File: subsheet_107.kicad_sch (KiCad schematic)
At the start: 17 parts, among them T12 BDX54

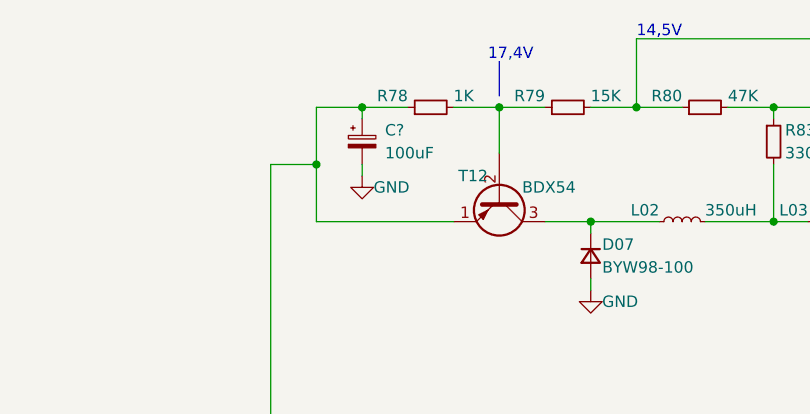
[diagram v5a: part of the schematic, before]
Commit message: fixes DRC : duplicate, designators with '?'
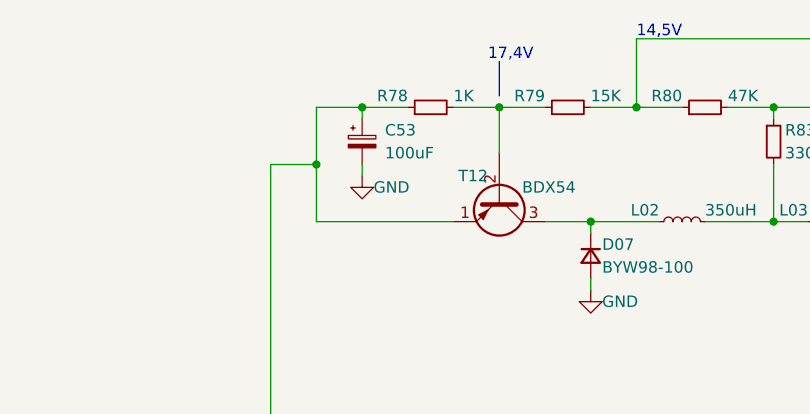
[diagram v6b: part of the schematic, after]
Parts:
- gave numbers to parts that had none: 1
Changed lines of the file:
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@@
   (symbol (lib_id "power-custom:+18V") (at 154.94 93.98 0) (unit 1)
     (in_bom yes) (on_board yes)
-    (property "Reference" "#PWR?" (id 0) (at 154.94 97.79 0)
+    (property "Reference" "#PWR0283" (id 0) (at 154.94 97.79 0)
       (effects (font (size 1.27 1.27)) hide)
     )
@@
   (symbol (lib_id "power:GND") (at 76.2 111.76 0) (unit 1)
     (in_bom yes) (on_board yes)
-    (property "Reference" "#PWR?" (id 0) (at 76.2 118.11 0)
+    (property "Reference" "#PWR0287" (id 0) (at 76.2 118.11 0)
       (effects (font (size 1.27 1.27)) hide)
     )
@@
   (symbol (lib_id "power-custom:+18V") (at 55.88 101.6 0) (unit 1)
     (in_bom yes) (on_board yes)
-    (property "Reference" "#PWR?" (id 0) (at 55.88 105.41 0)
+    (property "Reference" "#PWR0286" (id 0) (at 55.88 105.41 0)
       (effects (font (size 1.27 1.27)) hide)
     )
@@
   (symbol (lib_id "Device:C_Polarized_Small") (at 76.2 50.8 0) (unit 1)
     (in_bom yes) (on_board yes)
-    (property "Reference" "C?" (id 0) (at 78.74 49.53 0)
+    (property "Reference" "C53" (id 0) (at 78.74 49.53 0)
       (effects (font (size 1.27 1.27)) (justify left))
     )
@@
   (symbol (lib_id "power:+5V") (at 143.51 59.69 0) (unit 1)
     (in_bom yes) (on_board yes)
-    (property "Reference" "#PWR?" (id 0) (at 143.51 63.5 0)
+    (property "Reference" "#PWR0289" (id 0) (at 143.51 63.5 0)
       (effects (font (size 1.27 1.27)) hide)
     )
@@
   (symbol (lib_id "power:PWR_FLAG") (at 137.16 59.69 180) (unit 1)
     (in_bom yes) (on_board yes)
-    (property "Reference" "#FLG?" (id 0) (at 137.16 61.595 0)
+    (property "Reference" "#FLG0101" (id 0) (at 137.16 61.595 0)
       (effects (font (size 1.27 1.27)) hide)
     )
@@
   (symbol (lib_id "power:GND") (at 46.99 96.52 0) (unit 1)
     (in_bom yes) (on_board yes)
-    (property "Reference" "#PWR?" (id 0) (at 46.99 102.87 0)
+    (property "Reference" "#PWR0288" (id 0) (at 46.99 102.87 0)
       (effects (font (size 1.27 1.27)) hide)
     )
@@
   (symbol (lib_id "power:GND") (at 153.67 57.15 0) (unit 1)
     (in_bom yes) (on_board yes)
-    (property "Reference" "#PWR?" (id 0) (at 153.67 63.5 0)
+    (property "Reference" "#PWR0291" (id 0) (at 153.67 63.5 0)
       (effects (font (size 1.27 1.27)) hide)
     )
@@
   (symbol (lib_id "power:PWR_FLAG") (at 41.91 96.52 0) (unit 1)
     (in_bom yes) (on_board yes)
-    (property "Reference" "#FLG?" (id 0) (at 41.91 94.615 0)
+    (property "Reference" "#FLG0102" (id 0) (at 41.91 94.615 0)
       (effects (font (size 1.27 1.27)) hide)
     )
@@
   (symbol (lib_id "power:GND") (at 76.2 54.61 0) (unit 1)
     (in_bom yes) (on_board yes)
-    (property "Reference" "#PWR?" (id 0) (at 76.2 60.96 0)
+    (property "Reference" "#PWR0285" (id 0) (at 76.2 60.96 0)
       (effects (font (size 1.27 1.27)) hide)
     )
@@
   (symbol (lib_id "power:GND") (at 143.51 72.39 0) (unit 1)
     (in_bom yes) (on_board yes)
-    (property "Reference" "#PWR?" (id 0) (at 143.51 78.74 0)
+    (property "Reference" "#PWR0290" (id 0) (at 143.51 78.74 0)
       (effects (font (size 1.27 1.27)) hide)
     )
@@
   (symbol (lib_id "power:PWR_FLAG") (at 50.8 101.6 180) (unit 1)
     (in_bom yes) (on_board yes)
-    (property "Reference" "#FLG?" (id 0) (at 50.8 103.505 0)
+    (property "Reference" "#FLG0103" (id 0) (at 50.8 103.505 0)
       (effects (font (size 1.27 1.27)) hide)
     )
@@
   (symbol (lib_id "power:GND") (at 101.6 67.31 0) (unit 1)
     (in_bom yes) (on_board yes)
-    (property "Reference" "#PWR?" (id 0) (at 101.6 73.66 0)
-      (effects (font (size 1.27 1.27)) hide)
-    )
+    (property "Reference" "#PWR0284" (id 0) (at 101.6 73.66 0)
+      (effects (font (size 1.27 1.27)) hide)
+    )

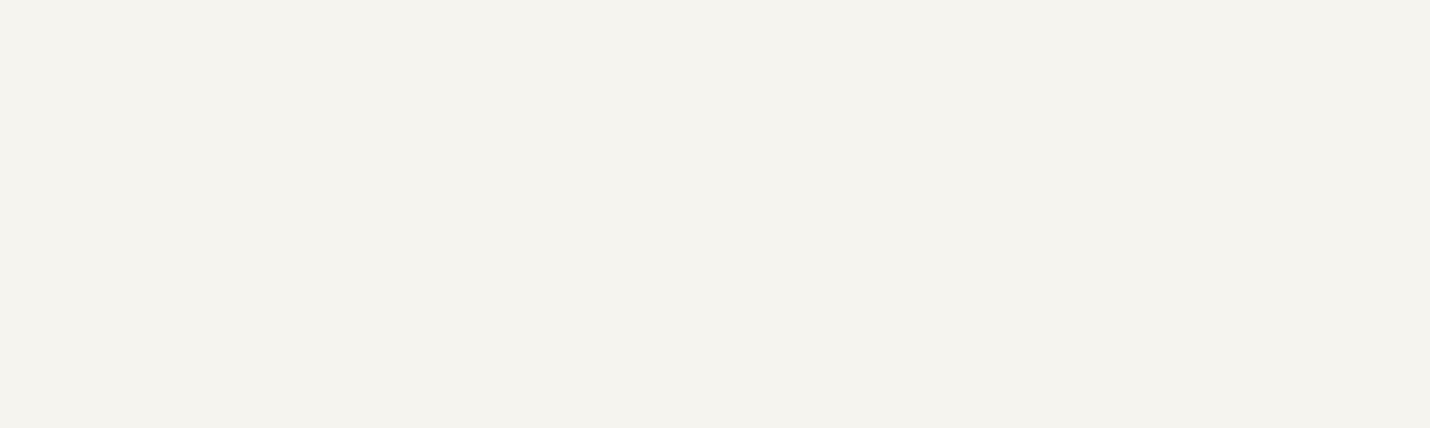
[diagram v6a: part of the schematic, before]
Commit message: schematic : mounting holes
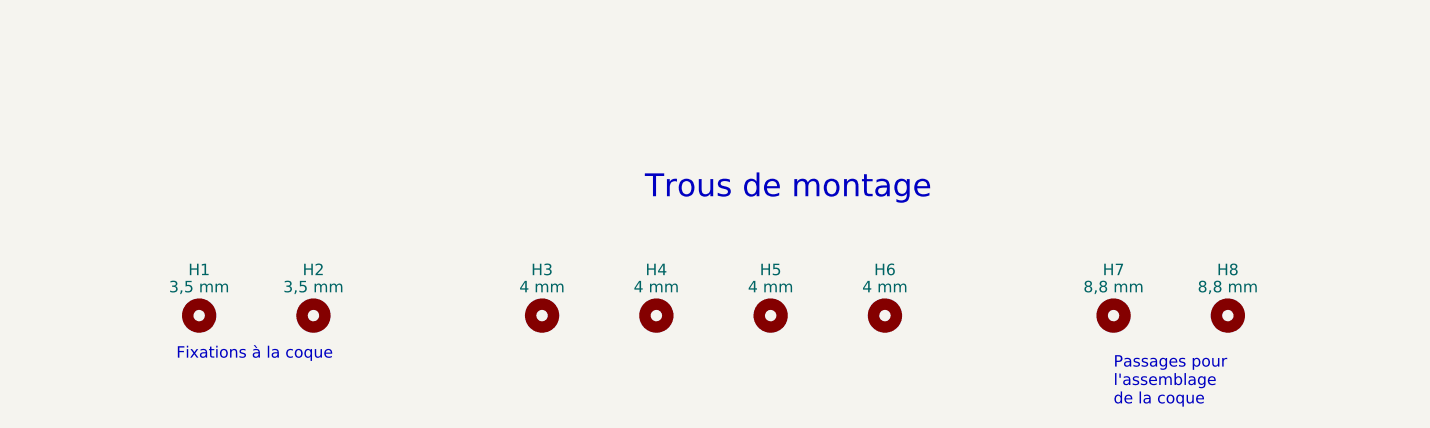
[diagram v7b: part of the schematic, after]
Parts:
- added H1, H2: 3,5 mm, mounting-holes-mo5:MountingHole_3.5mm_limited_courtyard, symbol Mechanical:MountingHole
- added H3, H4, H5, H6: 4 mm, mounting-holes-mo5:MountingHole_4mm_limited_courtyard, symbol Mechanical:MountingHole
- added H7, H8: 8,8 mm, mounting-holes-mo5:MountingHole_8.8mm_limited_courtyard, symbol Mechanical:MountingHole
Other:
- note added: "Fixations à la coque"
- note added: "Passages pour l'assemblage de la coque"
- note added: "Trous de montage"
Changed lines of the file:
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@@
     (effects (font (size 1.27 1.27)) (justify left bottom))
+  )
+  (text "Trous de montage" (at 87.63 203.2 0)
+    (effects (font (size 2.54 2.54)) (justify left bottom))
   )
   (text "17,4V" (at 90.17 41.91 0)
@@
     (effects (font (size 1.27 1.27)) (justify left bottom))
   )
+  (text "Fixations à la coque" (at 35.56 220.98 0)
+    (effects (font (size 1.27 1.27)) (justify left bottom))
+  )
   (text "5V" (at 83.82 104.14 0)
     (effects (font (size 1.27 1.27)) (justify left bottom))
@@
     (effects (font (size 1.27 1.27)) (justify right bottom))
   )
+  (text "Passages pour \nl'assemblage \nde la coque" (at 139.7 226.06 0)
+    (effects (font (size 1.27 1.27)) (justify left bottom))
+  )
   (text "5V" (at 107.95 99.06 180)
     (effects (font (size 1.27 1.27)) (justify right bottom))
@@
     )
     (pin "1")
+  )
+  (symbol (lib_id "Mechanical:MountingHole") (at 101.6 215.9 0) (unit 1)
+    (in_bom yes) (on_board yes)
+    (property "Reference" "H5" (id 0) (at 101.6 210.82 0))
+    (property "Value" "4 mm" (id 1) (at 101.6 212.725 0))
+    (property "Footprint" "mounting-holes-mo5:MountingHole_4mm_limited_courtyard" (id 2) (at 101.6 215.9 0)
+      (effects (font (size 1.27 1.27)) hide)
+    )
+    (property "Datasheet" "~" (id 3) (at 101.6 215.9 0)
+      (effects (font (size 1.27 1.27)) hide)
+    )
   )
   (symbol (lib_id "power:GND") (at 76.2 111.76 0) (unit 1)
@@
     (pin "1")
     (pin "2")
+  )
+  (symbol (lib_id "Mechanical:MountingHole") (at 114.3 215.9 0) (unit 1)
+    (in_bom yes) (on_board yes)
+    (property "Reference" "H6" (id 0) (at 114.3 210.82 0))
+    (property "Value" "4 mm" (id 1) (at 114.3 212.725 0))
+    (property "Footprint" "mounting-holes-mo5:MountingHole_4mm_limited_courtyard" (id 2) (at 114.3 215.9 0)
+      (effects (font (size 1.27 1.27)) hide)
+    )
+    (property "Datasheet" "~" (id 3) (at 114.3 215.9 0)
+      (effects (font (size 1.27 1.27)) hide)
+    )
   )
   (symbol (lib_id "Device:C_Polarized_Small") (at 76.2 50.8 0) (unit 1)
@@
     (pin "8")
   )
+  (symbol (lib_id "Mechanical:MountingHole") (at 139.7 215.9 0) (unit 1)
+    (in_bom yes) (on_board yes)
+    (property "Reference" "H7" (id 0) (at 139.7 210.82 0))
+    (property "Value" "8,8 mm" (id 1) (at 139.7 212.725 0))
+    (property "Footprint" "mounting-holes-mo5:MountingHole_8.8mm_limited_courtyard" (id 2) (at 139.7 215.9 0)
+      (effects (font (size 1.27 1.27)) hide)
+    )
+    (property "Datasheet" "~" (id 3) (at 139.7 215.9 0)
+      (effects (font (size 1.27 1.27)) hide)
+    )
+  )
   (symbol (lib_id "power:+5V") (at 143.51 59.69 0) (unit 1)
     (in_bom yes) (on_board yes)
@@
     )
     (pin "1")
+  )
+  (symbol (lib_id "Mechanical:MountingHole") (at 76.2 215.9 0) (unit 1)
+    (in_bom yes) (on_board yes)
+    (property "Reference" "H3" (id 0) (at 76.2 210.82 0))
+    (property "Value" "4 mm" (id 1) (at 76.2 212.725 0))
+    (property "Footprint" "mounting-holes-mo5:MountingHole_4mm_limited_courtyard" (id 2) (at 76.2 215.9 0)
+      (effects (font (size 1.27 1.27)) hide)
+    )
+    (property "Datasheet" "~" (id 3) (at 76.2 215.9 0)
+      (effects (font (size 1.27 1.27)) hide)
+    )
   )
   (symbol (lib_id "Device:C_Polarized_Small") (at 88.9 105.41 0) (unit 1)
@@
     (pin "2")
   )
+  (symbol (lib_id "Mechanical:MountingHole") (at 88.9 215.9 0) (unit 1)
+    (in_bom yes) (on_board yes)
+    (property "Reference" "H4" (id 0) (at 88.9 210.82 0))
+    (property "Value" "4 mm" (id 1) (at 88.9 212.725 0))
+    (property "Footprint" "mounting-holes-mo5:MountingHole_4mm_limited_courtyard" (id 2) (at 88.9 215.9 0)
+      (effects (font (size 1.27 1.27)) hide)
+    )
+    (property "Datasheet" "~" (id 3) (at 88.9 215.9 0)
+      (effects (font (size 1.27 1.27)) hide)
+    )
+  )
   (symbol (lib_id "power:GND") (at 153.67 57.15 0) (unit 1)
     (in_bom yes) (on_board yes)
@@
     (pin "1")
   )
+  (symbol (lib_id "Mechanical:MountingHole") (at 152.4 215.9 0) (unit 1)
+    (in_bom yes) (on_board yes)
+    (property "Reference" "H8" (id 0) (at 152.4 210.82 0))
+    (property "Value" "8,8 mm" (id 1) (at 152.4 212.725 0))
+    (property "Footprint" "mounting-holes-mo5:MountingHole_8.8mm_limited_courtyard" (id 2) (at 152.4 215.9 0)
+      (effects (font (size 1.27 1.27)) hide)
+    )
+    (property "Datasheet" "~" (id 3) (at 152.4 215.9 0)
+      (effects (font (size 1.27 1.27)) hide)
+    )
+  )
   (symbol (lib_id "Regulator_Linear:L78L05_TO92") (at 76.2 101.6 0) (unit 1)
     (in_bom yes) (on_board yes)
@@
     (pin "2")
   )
+  (symbol (lib_id "Mechanical:MountingHole") (at 38.1 215.9 0) (unit 1)
+    (in_bom yes) (on_board yes)
+    (property "Reference" "H1" (id 0) (at 38.1 210.82 0))
+    (property "Value" "3,5 mm" (id 1) (at 38.1 212.725 0))
+    (property "Footprint" "mounting-holes-mo5:MountingHole_3.5mm_limited_courtyard" (id 2) (at 38.1 215.9 0)
+      (effects (font (size 1.27 1.27)) hide)
+    )
+    (property "Datasheet" "~" (id 3) (at 38.1 215.9 0)
+      (effects (font (size 1.27 1.27)) hide)
+    )
+  )
+  (symbol (lib_id "Mechanical:MountingHole") (at 50.8 215.9 0) (unit 1)
+    (in_bom yes) (on_board yes)
+    (property "Reference" "H2" (id 0) (at 50.8 210.82 0))
+    (property "Value" "3,5 mm" (id 1) (at 50.8 212.725 0))
+    (property "Footprint" "mounting-holes-mo5:MountingHole_3.5mm_limited_courtyard" (id 2) (at 50.8 215.9 0)
+      (effects (font (size 1.27 1.27)) hide)
+    )
+    (property "Datasheet" "~" (id 3) (at 50.8 215.9 0)
+      (effects (font (size 1.27 1.27)) hide)
+    )
+  )
   (symbol (lib_id "Device:Q_PNP_EBC") (at 91.44 57.15 270) (unit 1)

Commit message: start association symbols-footprints
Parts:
- C53, C54: footprint (none) -> commons-passives_THT:Passive_THT_capacitor_polarized_EU_W2.54mm_L5.08mm
- C55: footprint (none) -> Capacitor_THT:CP_Radial_D10.0mm_P5.00mm
- C56: footprint (none) -> Capacitor_THT:CP_Radial_D13.0mm_P5.00mm
- R78, R79, R80, R81, R83: footprint (none) -> commons-passives_THT:Passive_THT_resistor_EU_W2.54mm_L12.70mm
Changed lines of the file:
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@@
       (effects (font (size 1.27 1.27)) (justify left))
     )
-    (property "Footprint" "" (id 2) (at 143.51 68.58 0)
+    (property "Footprint" "Capacitor_THT:CP_Radial_D13.0mm_P5.00mm" (id 2) (at 143.51 68.58 0)
       (effects (font (size 1.27 1.27)) hide)
     )
@@
       (effects (font (size 1.27 1.27)) (justify left))
     )
-    (property "Footprint" "" (id 2) (at 153.67 53.34 0)
+    (property "Footprint" "Capacitor_THT:CP_Radial_D10.0mm_P5.00mm" (id 2) (at 153.67 53.34 0)
       (effects (font (size 1.27 1.27)) hide)
     )
@@
       (effects (font (size 1.27 1.27)) (justify right))
     )
-    (property "Footprint" "" (id 2) (at 96.52 101.6 0)
+    (property "Footprint" "commons-passives_THT:Passive_THT_resistor_EU_W2.54mm_L12.70mm" (id 2) (at 96.52 101.6 0)
       (effects (font (size 1.27 1.27)) hide)
     )
@@
       (effects (font (size 1.27 1.27)) (justify right))
     )
-    (property "Footprint" "" (id 2) (at 114.3 46.99 0)
+    (property "Footprint" "commons-passives_THT:Passive_THT_resistor_EU_W2.54mm_L12.70mm" (id 2) (at 114.3 46.99 0)
       (effects (font (size 1.27 1.27)) hide)
     )
@@
       (effects (font (size 1.27 1.27)) (justify left))
     )
-    (property "Footprint" "" (id 2) (at 76.2 50.8 0)
+    (property "Footprint" "commons-passives_THT:Passive_THT_capacitor_polarized_EU_W2.54mm_L5.08mm" (id 2) (at 76.2 50.8 0)
       (effects (font (size 1.27 1.27)) hide)
     )
@@
       (effects (font (size 1.27 1.27)) (justify right))
     )
-    (property "Footprint" "" (id 2) (at 99.06 46.99 0)
+    (property "Footprint" "commons-passives_THT:Passive_THT_resistor_EU_W2.54mm_L12.70mm" (id 2) (at 99.06 46.99 0)
       (effects (font (size 1.27 1.27)) hide)
     )
@@
       (effects (font (size 1.27 1.27)) (justify right))
     )
-    (property "Footprint" "" (id 2) (at 83.82 46.99 0)
+    (property "Footprint" "commons-passives_THT:Passive_THT_resistor_EU_W2.54mm_L12.70mm" (id 2) (at 83.82 46.99 0)
       (effects (font (size 1.27 1.27)) hide)
     )
@@
       (effects (font (size 1.27 1.27)) (justify left))
     )
-    (property "Footprint" "" (id 2) (at 88.9 105.41 0)
+    (property "Footprint" "commons-passives_THT:Passive_THT_capacitor_polarized_EU_W2.54mm_L5.08mm" (id 2) (at 88.9 105.41 0)
       (effects (font (size 1.27 1.27)) hide)
     )
@@
       (effects (font (size 1.27 1.27)) (justify left))
     )
-    (property "Footprint" "" (id 2) (at 121.92 50.8 0)
-      (effects (font (size 1.27 1.27)) hide)
-    )
+    (property "Footprint" "commons-passives_THT:Passive_THT_resistor_EU_W2.54mm_L12.70mm" (id 2) (at 121.92 50.8 0)
+      (effects (font (size 1.27 1.27)) hide)
+    )
